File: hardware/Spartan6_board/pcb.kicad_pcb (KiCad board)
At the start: 4 copper layers, 69.6 x 29.4 mm, 169 parts, among them J1 USB_C_Receptacle_USB2.0, J10 TF TF-018 1.5mm, J5 SWD, J6 DF12NB(3.0)-30DS-0.5V(51), J7 DF12NB(3.0)-30DS-0.5V(51), J8 JTAG, J9 Conn_01x20, Q3 AO3400A, Q4 AO3400A, Q5 AO3400A, SW1 TS-1007S-AR02516, SW2 TS-1007S-AR02516, U1 SY8120, U12 MT41K64M16TW, U13 W25Q32JV, U14 RP2040, U15 USBLC6-2P6, U2 SY8120, U3 SY8120, U4 MT9700, U5 XC6SLX16-FTG256, U6 MT9700-N, Y1 33MHz, Y2 12MHz

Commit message: fixed mixup of pins G5/G4 (3rd diff pair ODD) and DE/PCLK (3rd diff pair EVEN), now with correct polarity for diff pairs
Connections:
- J6 pad 4: G4 -> G5
- J6 pad 6: G5 -> G4
- U5 pad P15: G5 -> G4
- U5 pad P16: G4 -> G5
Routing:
- net G5: track 9.68 -> 8.63 mm
- net G4: track 8.63 -> 9.68 mm
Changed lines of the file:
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@@
 			(size 0.4 0.4)
 			(layers "F.Cu" "F.Paste" "F.Mask")
-			(net 79 "G5")
+			(net 84 "G4")
 			(pinfunction "IO_L48P_HDC_M1DQ8_1")
 			(pintype "bidirectional")
@@
 			(size 0.4 0.4)
 			(layers "F.Cu" "F.Paste" "F.Mask")
-			(net 84 "G4")
+			(net 79 "G5")
 			(pinfunction "IO_L48N_M1DQ9_1")
 			(pintype "bidirectional")
@@
 			(size 0.3 1.6)
 			(layers "B.Cu" "B.Paste" "B.Mask")
-			(net 84 "G4")
+			(net 79 "G5")
 			(pinfunction "3")
 			(pintype "passive")
@@
 			(size 0.3 1.6)
 			(layers "B.Cu" "B.Paste" "B.Mask")
-			(net 79 "G5")
+			(net 84 "G4")
 			(pinfunction "5")
 			(pintype "passive")
@@
 	)
 	(segment
-		(start 167.00041 67.149184)
-		(end 164.50041 69.649184)
+		(start 164.40041 69.349184)
+		(end 161.80041 69.349184)
 		(width 0.11)
 		(layer "F.Cu")
@@
 	)
 	(segment
-		(start 161.10041 69.649184)
-		(end 160.60041 69.149184)
+		(start 161.80041 69.349184)
+		(end 161.60041 69.149184)
 		(width 0.11)
 		(layer "F.Cu")
@@
 	)
 	(segment
-		(start 164.50041 69.649184)
-		(end 161.10041 69.649184)
+		(start 167.50041 66.649184)
+		(end 167.10041 66.649183)
 		(width 0.11)
 		(layer "F.Cu")
@@
 	)
 	(segment
-		(start 167.20041 67.149184)
-		(end 167.00041 67.149184)
+		(start 167.10041 66.649183)
+		(end 164.40041 69.349184)
 		(width 0.11)
 		(layer "F.Cu")
@@
 	)
 	(via
-		(at 167.20041 67.149184)
+		(at 167.50041 66.649184)
 		(size 0.45)
 		(drill 0.2)
@@
 	)
 	(segment
-		(start 167.40041 67.349184)
-		(end 168.95041 67.349185)
+		(start 167.50041 66.649184)
+		(end 167.70041 66.849184)
 		(width 0.11)
 		(layer "B.Cu")
@@
 	)
 	(segment
-		(start 167.20041 67.149184)
-		(end 167.40041 67.349184)
+		(start 167.70041 66.849184)
+		(end 168.95041 66.849184)
 		(width 0.11)
 		(layer "B.Cu")
@@
 	)
 	(segment
-		(start 164.40041 69.349184)
-		(end 161.80041 69.349184)
+		(start 167.00041 67.149184)
+		(end 164.50041 69.649184)
 		(width 0.11)
 		(layer "F.Cu")
@@
 	)
 	(segment
-		(start 161.80041 69.349184)
-		(end 161.60041 69.149184)
+		(start 161.10041 69.649184)
+		(end 160.60041 69.149184)
 		(width 0.11)
 		(layer "F.Cu")
@@
 	)
 	(segment
-		(start 167.50041 66.649184)
-		(end 167.10041 66.649183)
+		(start 164.50041 69.649184)
+		(end 161.10041 69.649184)
 		(width 0.11)
 		(layer "F.Cu")
@@
 	)
 	(segment
-		(start 167.10041 66.649183)
-		(end 164.40041 69.349184)
+		(start 167.20041 67.149184)
+		(end 167.00041 67.149184)
 		(width 0.11)
 		(layer "F.Cu")
@@
 	)
 	(via
-		(at 167.50041 66.649184)
+		(at 167.20041 67.149184)
 		(size 0.45)
 		(drill 0.2)
@@
 	)
 	(segment
-		(start 167.50041 66.649184)
-		(end 167.70041 66.849184)
+		(start 167.40041 67.349184)
+		(end 168.95041 67.349185)
 		(width 0.11)
 		(layer "B.Cu")
@@
 	)
 	(segment
-		(start 167.70041 66.849184)
-		(end 168.95041 66.849184)
+		(start 167.20041 67.149184)
+		(end 167.40041 67.349184)
 		(width 0.11)
 		(layer "B.Cu")

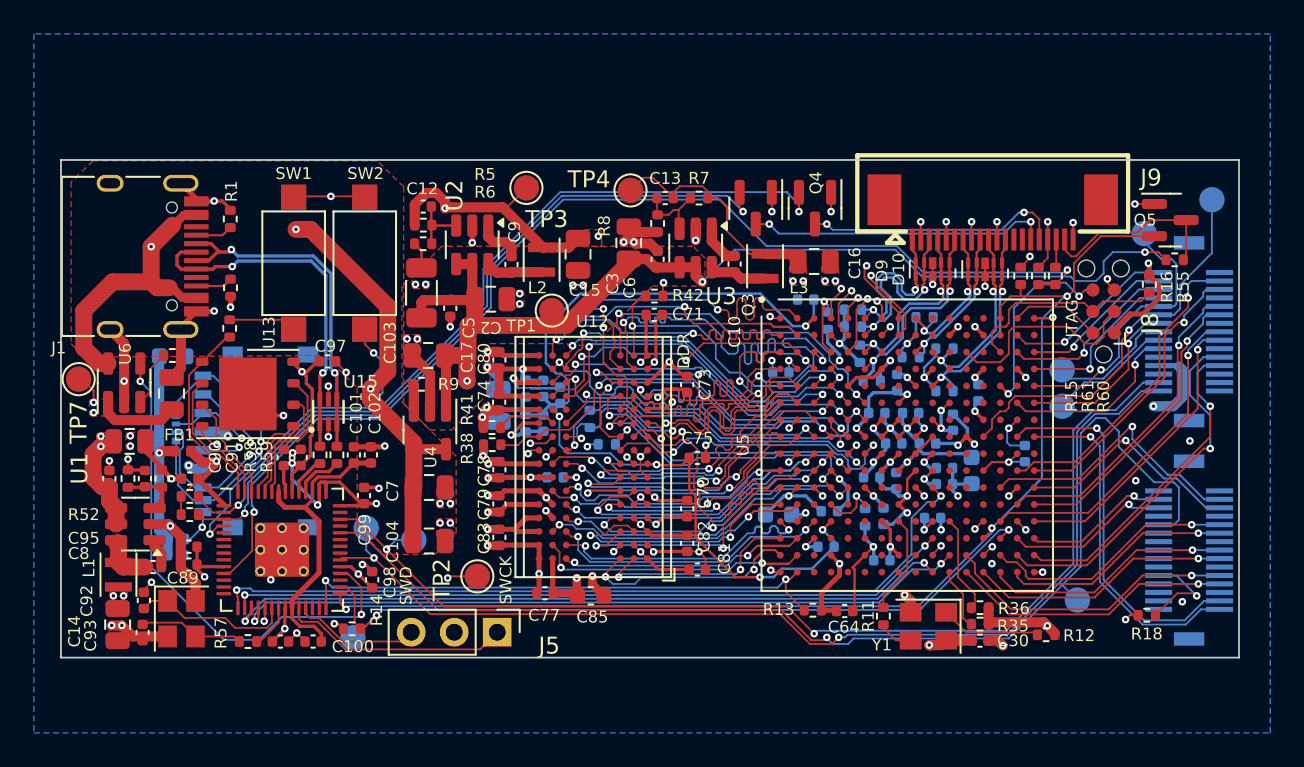
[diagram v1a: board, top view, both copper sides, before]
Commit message: change DVI FPC pinout to match DVI connector (G-S-S-G), and FPGA device from XC6SLX16-FTG256 to XC6SLX25-3FTG256C
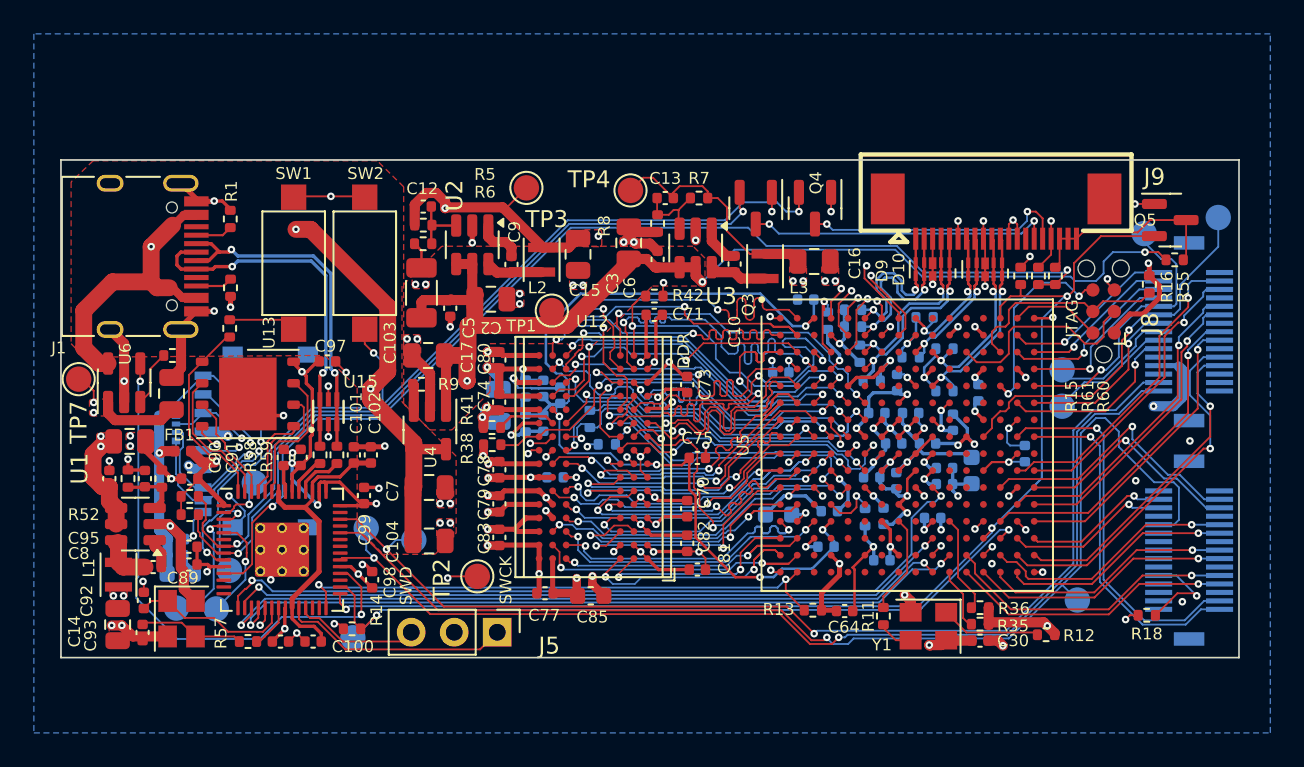
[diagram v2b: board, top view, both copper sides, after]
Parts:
- added TP14: TestPoint_Small, TestPoint:TestPoint_Pad_D1.5mm, B.Cu at (115.5, 65.9)
- added TP15: TestPoint_Small, TestPoint:TestPoint_Pad_D1.5mm, B.Cu at (114.0, 71.0)
- added TP16: TestPoint_Small, TestPoint:TestPoint_Pad_D1.5mm, B.Cu at (110.9, 73.3)
- added TP17: TestPoint_Small, TestPoint:TestPoint_Pad_D1.5mm, B.Cu at (113.3, 73.3)
- U5: value XC6SLX16-FTG256 -> XC6SLX25-3FTG256C
- moved C33 12.9 mm to (111.2, 71.2)
- moved TP5 1.12 mm to (172.5, 50.2)
- moved J9 0.21 mm to (159.3, 50.3)
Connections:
- J9 pad 11: GND -> TMDS_CKN
- J9 pad 12: TMDS_CKN -> GND
- J9 pad 13: unconnected-(J9-Pin_13-Pad13) -> GND
- J9 pad 14: unconnected-(J9-Pin_14-Pad14) -> Net-(J9-Pin_14)
- J9 pad 18: Net-(J9-Pin_18) -> /dp_in/HPD_5V
- J9 pad 2: GND -> TMDS_D2N
- J9 pad 20: GND -> /dp_in/HPD_5V
- J9 pad 3: TMDS_D2N -> GND
- J9 pad 5: GND -> TMDS_D1N
- J9 pad 6: TMDS_D1N -> GND
- J9 pad 8: GND -> TMDS_D0N
- J9 pad 9: TMDS_D0N -> GND
- R60 pad 1: Net-(J9-Pin_18) -> /dp_in/HPD_5V
- U14 pad 2: DDC_SDA -> /mcu/GPIO0
- U14 pad 3: DDC_SCL -> /mcu/GPIO1
- U14 pad 4: KEY -> /mcu/GPIO2
- U14 pad 7: /mcu/GPIO5 -> DDC_SDA
- U14 pad 8: /mcu/GPIO6 -> DDC_SCL
- U14 pad 9: /mcu/GPIO7 -> KEY
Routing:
- net +5V: track 96.6 -> 106.4 mm
- net /mcu/GPIO2: track 0.00 -> 7.17 mm, vias 0 -> 1
- net GND: track 193.8 -> 200.1 mm, vias 117 -> 116
- net /mcu/GPIO3: track 0.00 -> 6.26 mm, vias 0 -> 1
- net /mcu/GPIO1: track 0.00 -> 5.63 mm, vias 0 -> 1
- net /mcu/GPIO0: track 0.00 -> 3.15 mm, vias 0 -> 1
- net /dp_in/VDD_SD: track 19.9 -> 17.5 mm
- net KEY: track 19.7 -> 22.0 mm
- net DDC_SDA: track 47.5 -> 49.7 mm
- net HDMI_DET: track 66.8 -> 64.7 mm
- net EPD_PWR_EN: track 30.0 -> 31.8 mm
- net Net-(J9-Pin_18): track 1.66 -> 0.00 mm
- net DDC_SCL: track 44.2 -> 45.7 mm
- net /dp_in/HPD_5V: track 11.2 -> 12.1 mm
- net LCD_VSYNC: track 23.5 -> 22.6 mm
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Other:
- board text added: "FPGA small board v0.1"
- board text added: "VERSION:"

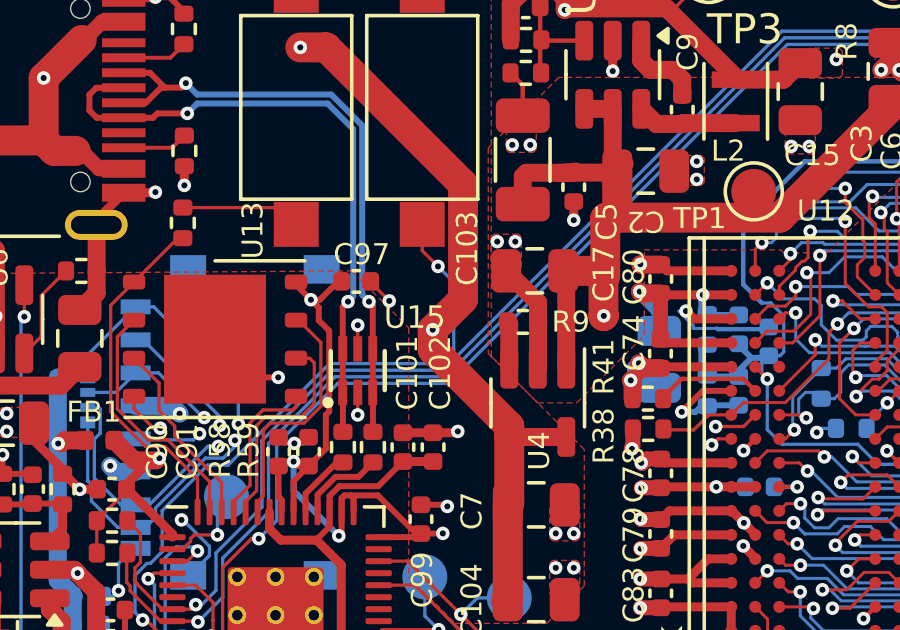
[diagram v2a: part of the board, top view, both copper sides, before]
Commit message: review and update manufacturing constraints (via size, etc.)
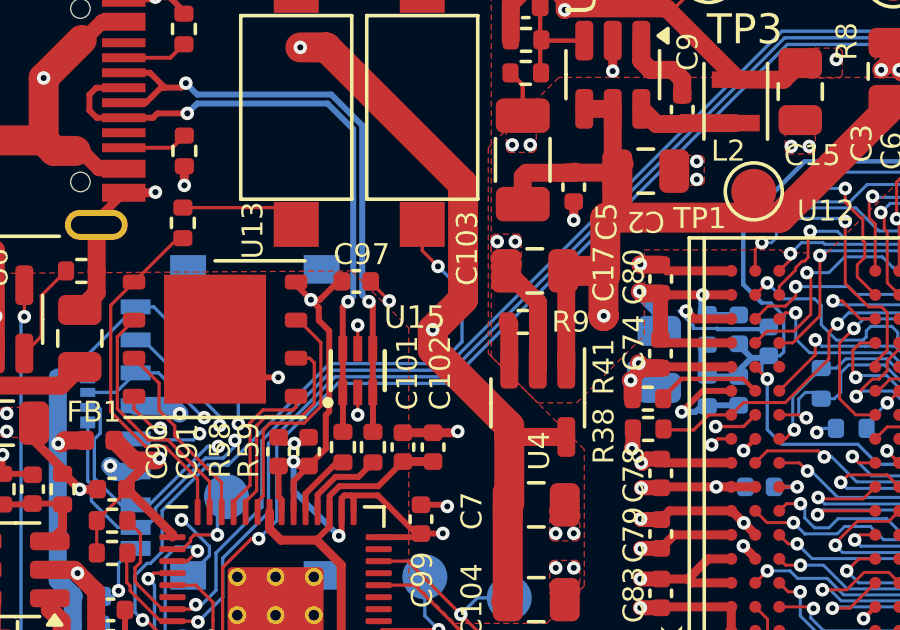
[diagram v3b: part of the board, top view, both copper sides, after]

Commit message: fix R0/R1 mixup
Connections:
- J6 pad 27: R1 -> R0
- J6 pad 29: R0 -> R1
- U5 pad H15: R1 -> R0
- U5 pad H16: R0 -> R1
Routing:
- net R1: track 22.3 -> 20.6 mm
- net R0: track 20.6 -> 22.3 mm

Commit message: fixes for producion and notes
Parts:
- TP7: moved to B.Cu
- moved TP6 2.55 mm to (169.1, 48.8)
- moved TP3 1.70 mm to (132.7, 49.8)
- moved TP5 1.43 mm to (172.0, 48.9)
- moved TP7 0.65 mm to (105.7, 59.4), turned to 90 degrees
- moved TP12 0.50 mm to (162.9, 61.8)
- moved R6 0.24 mm to (125.7, 51.7)
- moved R5 0.23 mm to (125.7, 50.6)
- moved C12 0.22 mm to (125.7, 49.5)
- moved TP4 0.18 mm to (137.6, 48.7)
- moved TP17 0.18 mm to (113.3, 73.5)
- moved TP16 0.15 mm to (110.8, 73.3)
- moved C68 0.10 mm to (148.0, 55.0)
- moved C33 0.10 mm to (111.2, 71.3)
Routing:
- net +3V3: track 108.0 -> 211.9 mm
- net +1V35: track 73.6 -> 152.4 mm
- net +1V0: track 34.5 -> 54.5 mm
- net +5V_OUT: track 86.3 -> 89.1 mm
- net GND: track 200.1 -> 198.0 mm
- net LCD_HSYNC: track 16.5 -> 18.3 mm
- net FPGA_DONE: track 72.8 -> 71.2 mm
- net Net-(U5A-IO_L1P_HSWAPEN_0): track 4.45 -> 3.01 mm
- net FPGA_TDO: track 11.6 -> 10.2 mm
- net LCD_VSYNC: track 22.6 -> 23.7 mm
- net SD0_DAT3: track 53.1 -> 53.7 mm
- net +5V: track 106.4 -> 107.0 mm
